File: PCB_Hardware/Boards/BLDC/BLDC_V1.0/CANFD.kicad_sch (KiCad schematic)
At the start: 11 parts, among them J1 Conn_01x04_Pin, J2 Conn_01x04_Pin, Q1 SI2302, U3 TCAN1044VDR

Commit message: Add DBcan transport refactor, BLDC V1.0 schematic + sim work, HAL submodule
- DBcan: replace bare-register driver with vendor-agnostic transport abstraction (core/, transports/, refactored bootloader driver, README)
- Add stm32g4xx_hal_driver as Firmware/libs submodule
- Add HAL config for BLDC board (stm32g4xx_hal_conf.h)
- BLDC V1.0: schematic edits across 10 sheets (footprint assignments, repositioning); design-doc README (gate-driver constraints, FET selection / TPH3R70APL, thermal analysis)
- ngspice simulation workflow (cap sweeps, half-bridge slow turn-on)
- Ignore .obsidian/ vault state and large simulation CSV exports
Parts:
- C2, C3, C4: footprint (none) -> Capacitor_SMD:C_0402_1005Metric
- D2, D3: footprint (none) -> Package_TO_SOT_SMD:SOT-23
- J1, J2: footprint (none) -> Connector_JST:JST_XH_S4B-XH-A-1_1x04_P2.50mm_Horizontal
- R1, R2: footprint (none) -> Resistor_SMD:R_0402_1005Metric
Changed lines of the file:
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@@
 			)
 		)
-		(property "Footprint" ""
+		(property "Footprint" "Connector_JST:JST_XH_S4B-XH-A-1_1x04_P2.50mm_Horizontal"
 			(at 212.09 109.22 0)
 			(hide yes)
@@
 			)
 		)
-		(property "Footprint" ""
+		(property "Footprint" "Resistor_SMD:R_0402_1005Metric"
 			(at 152.4 76.708 90)
 			(hide yes)
@@
 			)
 		)
-		(property "Footprint" ""
+		(property "Footprint" "Package_TO_SOT_SMD:SOT-23"
 			(at 151.13 104.14 0)
 			(hide yes)
@@
 			)
 		)
-		(property "Footprint" ""
+		(property "Footprint" "Capacitor_SMD:C_0402_1005Metric"
 			(at 106.3752 77.47 0)
 			(hide yes)
@@
 			)
 		)
-		(property "Footprint" ""
+		(property "Footprint" "Connector_JST:JST_XH_S4B-XH-A-1_1x04_P2.50mm_Horizontal"
 			(at 212.09 92.71 0)
 			(hide yes)
@@
 			)
 		)
-		(property "Footprint" ""
+		(property "Footprint" "Capacitor_SMD:C_0402_1005Metric"
 			(at 133.0452 77.47 0)
 			(hide yes)
@@
 			)
 		)
-		(property "Footprint" ""
+		(property "Footprint" "Package_TO_SOT_SMD:SOT-23"
 			(at 181.61 120.65 0)
 			(hide yes)
@@
 			)
 		)
-		(property "Footprint" ""
+		(property "Footprint" "Resistor_SMD:R_0402_1005Metric"
 			(at 162.56 76.708 90)
 			(hide yes)
@@
 			)
 		)
-		(property "Footprint" ""
+		(property "Footprint" "Capacitor_SMD:C_0402_1005Metric"
 			(at 158.4452 83.82 0)
 			(hide yes)

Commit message: Created organization around the symbol lib and did a first pass layout of the BDLC
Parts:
- added D19, D20: PESD5V0L1UL, Diode_SMD:D_SOD-882, symbol Diode:PESD5V0L1UL
- added Q14: SI2302, Package_TO_SOT_SMD:SOT-23, symbol Transistor_FET:Q_NMOS_GSD
- added R33: 1.8k, Resistor_SMD:R_0402_1005Metric, symbol Device:R
- added R34: 3.3k, Resistor_SMD:R_0402_1005Metric, symbol Device:R
- added R35: 10k, Resistor_SMD:R_0402_1005Metric, symbol Device:R
- added R36: 1k, Resistor_SMD:R_0402_1005Metric, symbol Device:R
- J1, J2: footprint Connector_JST:JST_XH_S4B-XH-A-1_1x04_P2.50mm_Horizontal -> DBRobot:CONN_JST_SM04B-PASS
- R1, R2: footprint Resistor_SMD:R_0402_1005Metric -> Resistor_SMD:R_0805_2012Metric
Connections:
- net +5V: now also R35.2
- net GND: now also D19.2 (A), D20.2 (A), Q14.2 (S), R34.1
- net SEQ1: now also R33.1, R34.2; no longer J1.3 (Pin_3)
- net SEQ2: now also Q14.1 (G); no longer J2.3 (Pin_3)
- net CAN+: now reaches D2.2 (A2), D3.2 (A2), J1.1 (Pin_1), J2.1 (Pin_1), R1.1, U3.7 (CANH)
- net CAN-: now reaches D2.1 (A1), D3.1 (A1), J1.2 (Pin_2), J2.2 (Pin_2), Q1.3 (D), U3.6 (CANL)
- net +3V3 renamed +3.3V
- new net: Q14.3 (D), R35.1, R36.2
- new net: D19.1 (K), J1.3 (Pin_3), R33.2
- new net: D20.1 (K), J2.3 (Pin_3), R36.1
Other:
- moved on the sheet: C2, C3, C4, D2, D3, J1, J2, Q1, R1, R2, U3

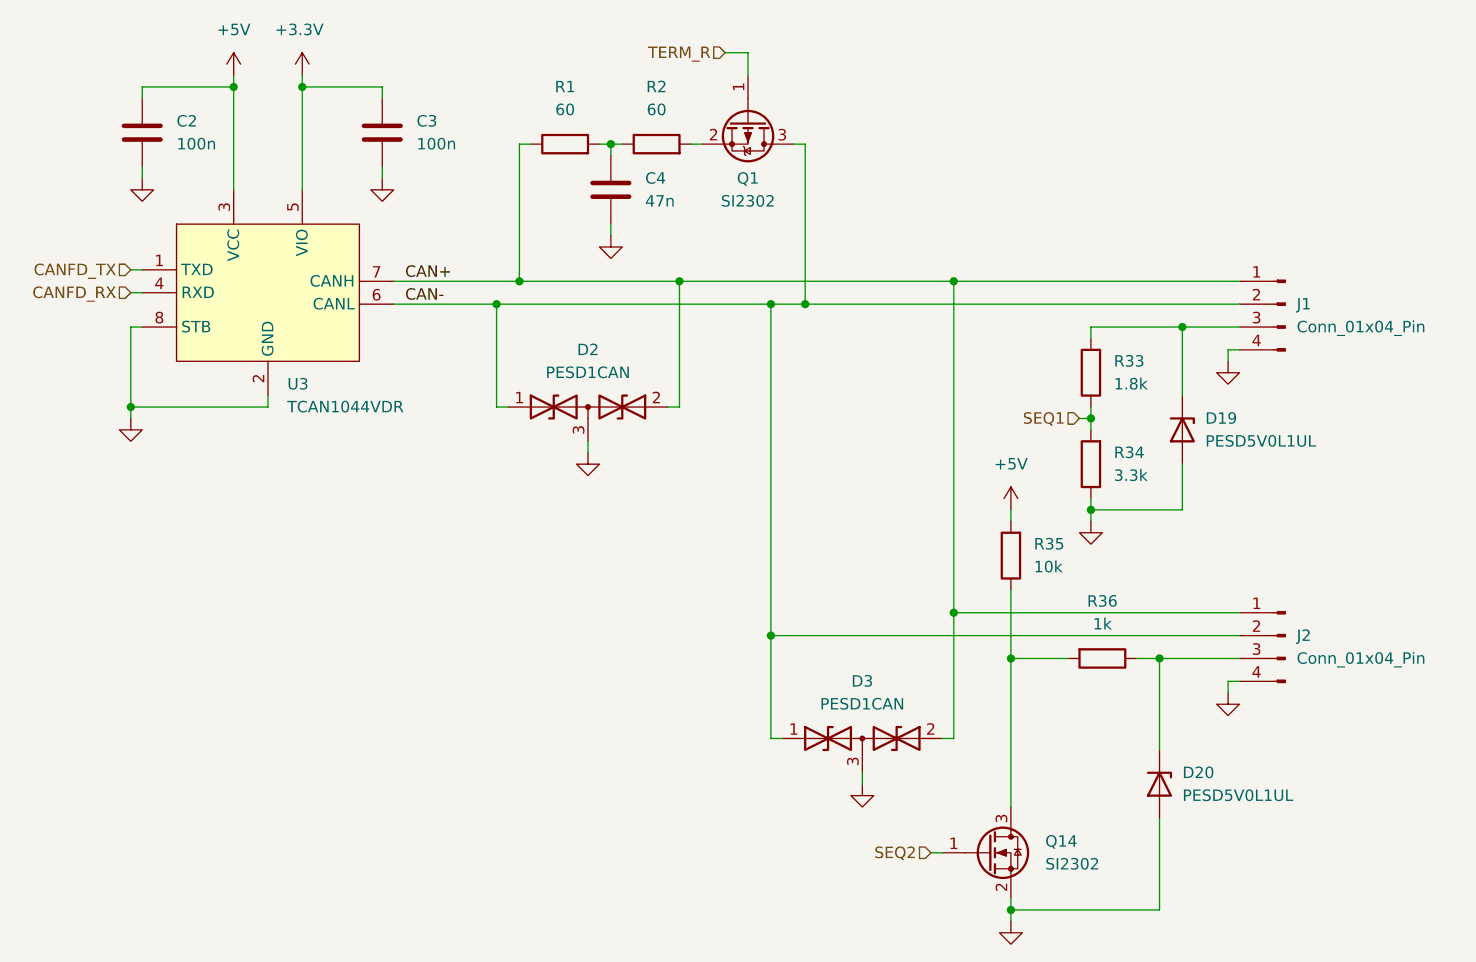
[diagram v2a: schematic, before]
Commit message: complete redo of the BLDC layout
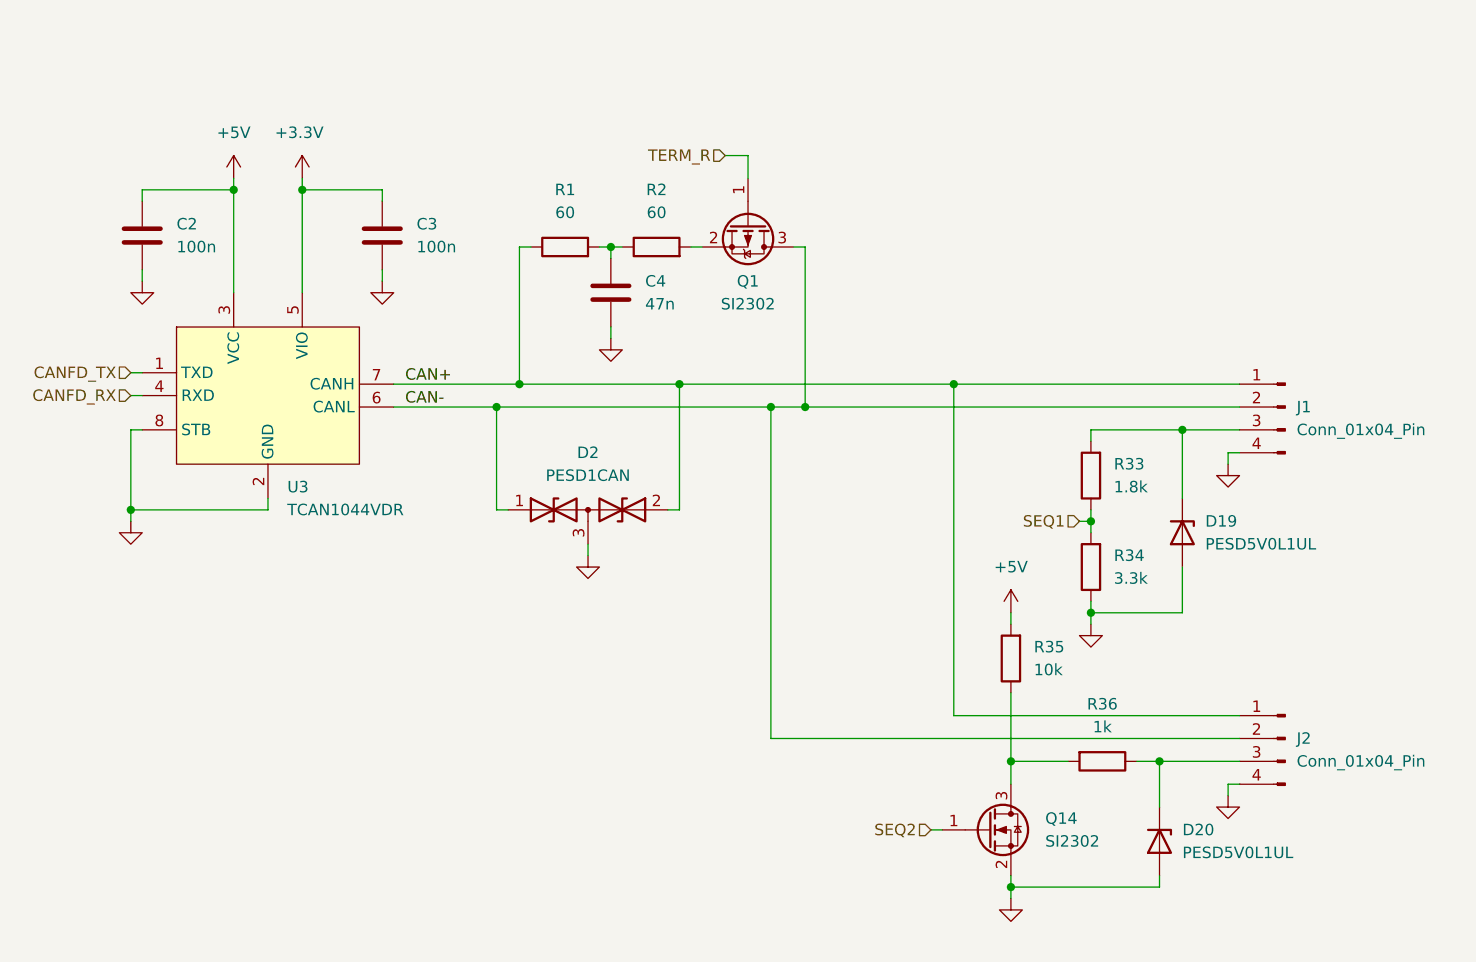
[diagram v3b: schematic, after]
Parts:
- removed D3: PESD1CAN, Package_TO_SOT_SMD:SOT-23, symbol Device:D_TVS_Dual_AAC
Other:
- moved on the sheet: C2, C3, C4, D19, D2, D20, J1, J2, Q1, Q14, R1, R2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
